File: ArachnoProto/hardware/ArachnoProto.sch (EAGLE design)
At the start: 21 parts, among them J1 PINHEAD-17-REV, J2 PINHEAD-17-REV

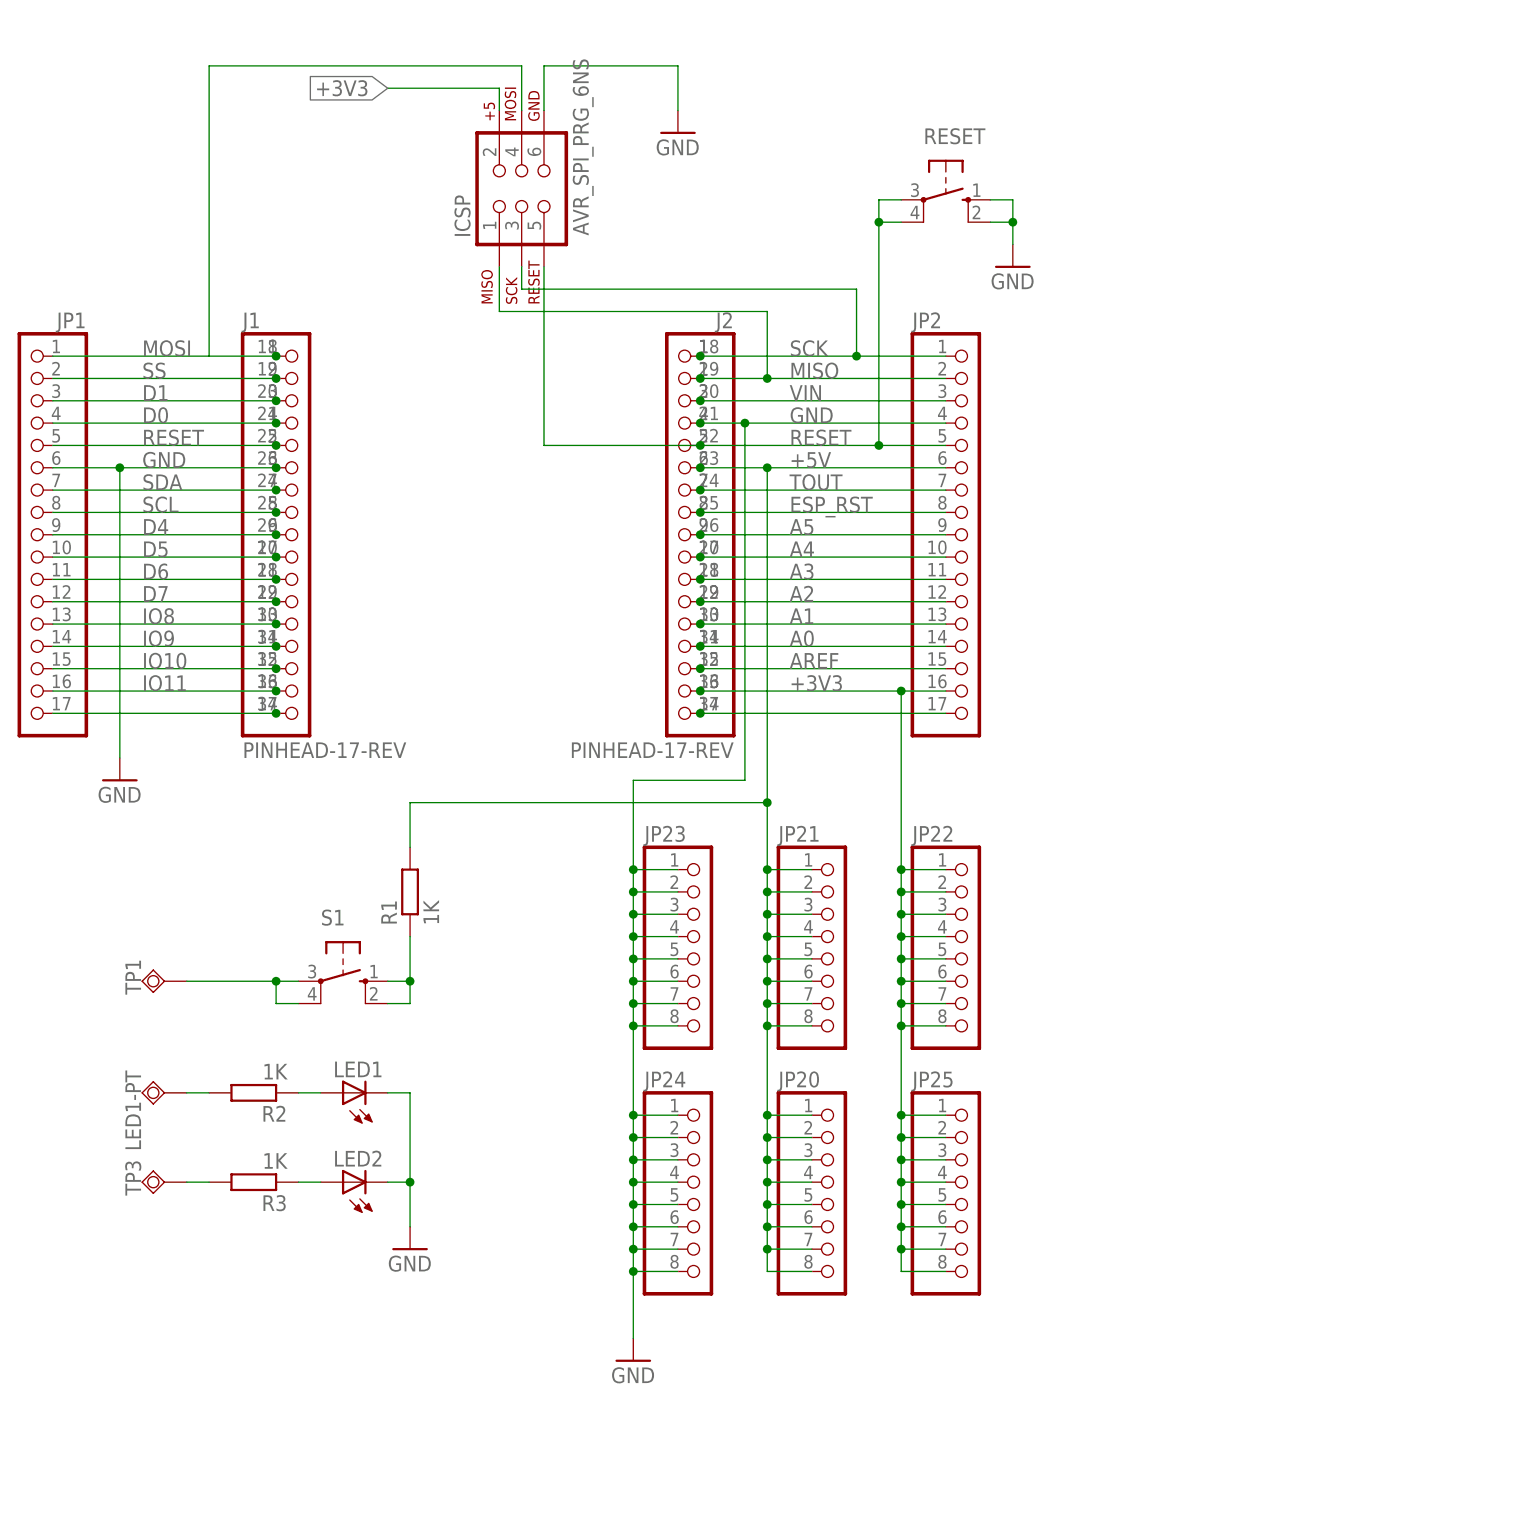
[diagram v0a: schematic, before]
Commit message: -- Added mounting pads on the board -- Made reset button an independent button -- Changed all components to SMD
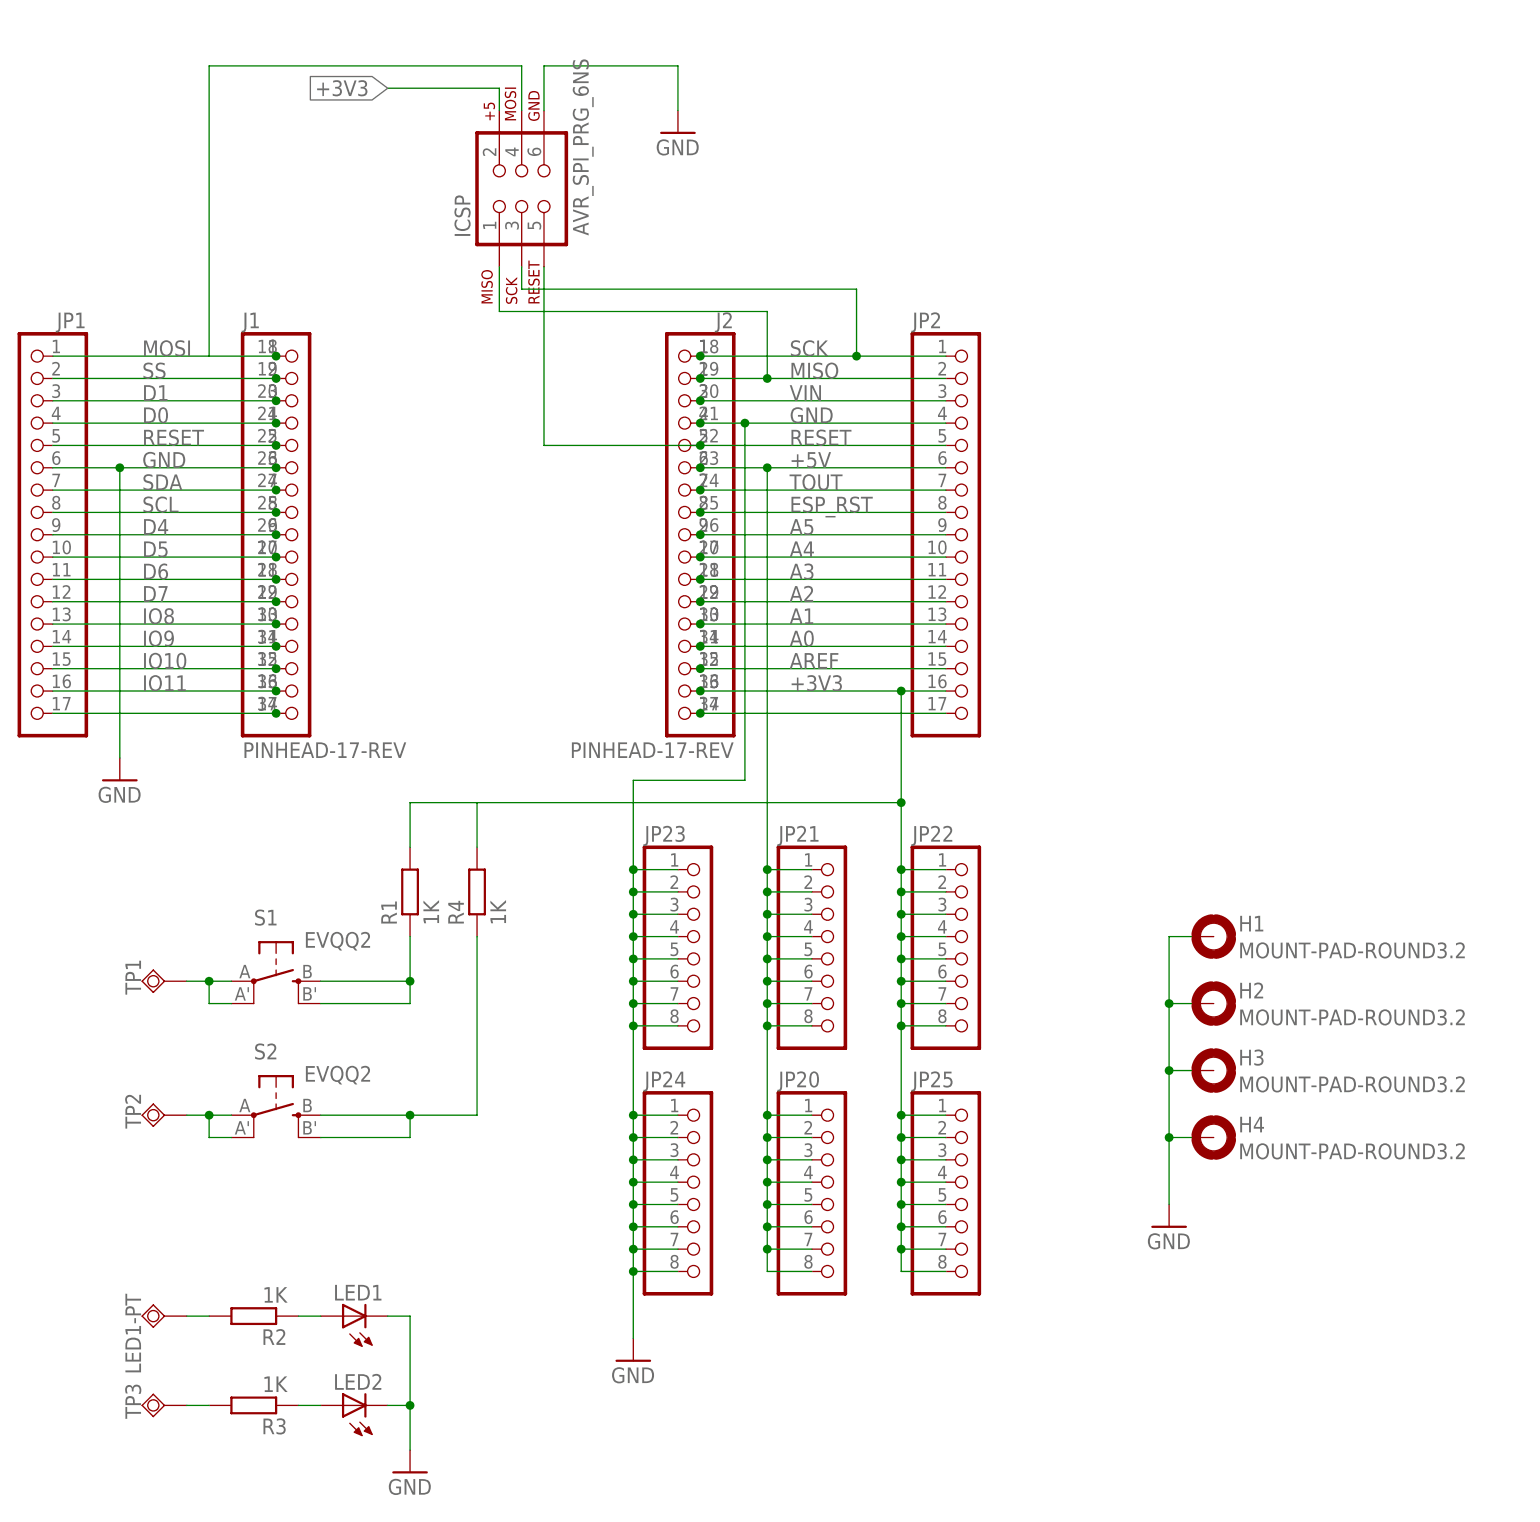
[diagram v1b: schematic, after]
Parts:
- removed RESET: (no value), switch-omron:10-XX
- added H1, H2, H3, H4: MOUNT-PAD-ROUND3.2, holes:MOUNT-PAD-ROUND3.2
- added R4: 1K, resistor:R-EU_R1206
- added S2: EVQQ2, adafruit:EVQQ2
- added TP2: TPSQPAD1-20Y, test-fixtures:TPSQPAD1-20Y
- LED1, LED2: device adafruit:LED5MM -> led:LEDCHIPLED_1206
- R1, R2, R3: device resistor:R-EU_R0603 -> resistor:R-EU_R1206
- S1: value (none) -> EVQQ2; device switch-omron:10-XX -> adafruit:EVQQ2
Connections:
- new net N$69: R4.1, S2.S, S2.S1
- new net N$70: S2.P, S2.P1, TP2.TP
- net +3V3: now also R1.2, R4.2
- net +5V: no longer R1.2
- net GND: now also H1.MOUNT, H2.MOUNT, H3.MOUNT, H4.MOUNT; no longer RESET.S, RESET.S1
- net RESET: no longer RESET.P, RESET.P1
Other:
- moved on the sheet: LED1, LED1-PT, LED2, R2, R3, TP3

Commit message: Modified ArachnoProto to work with the ArachnioDue.
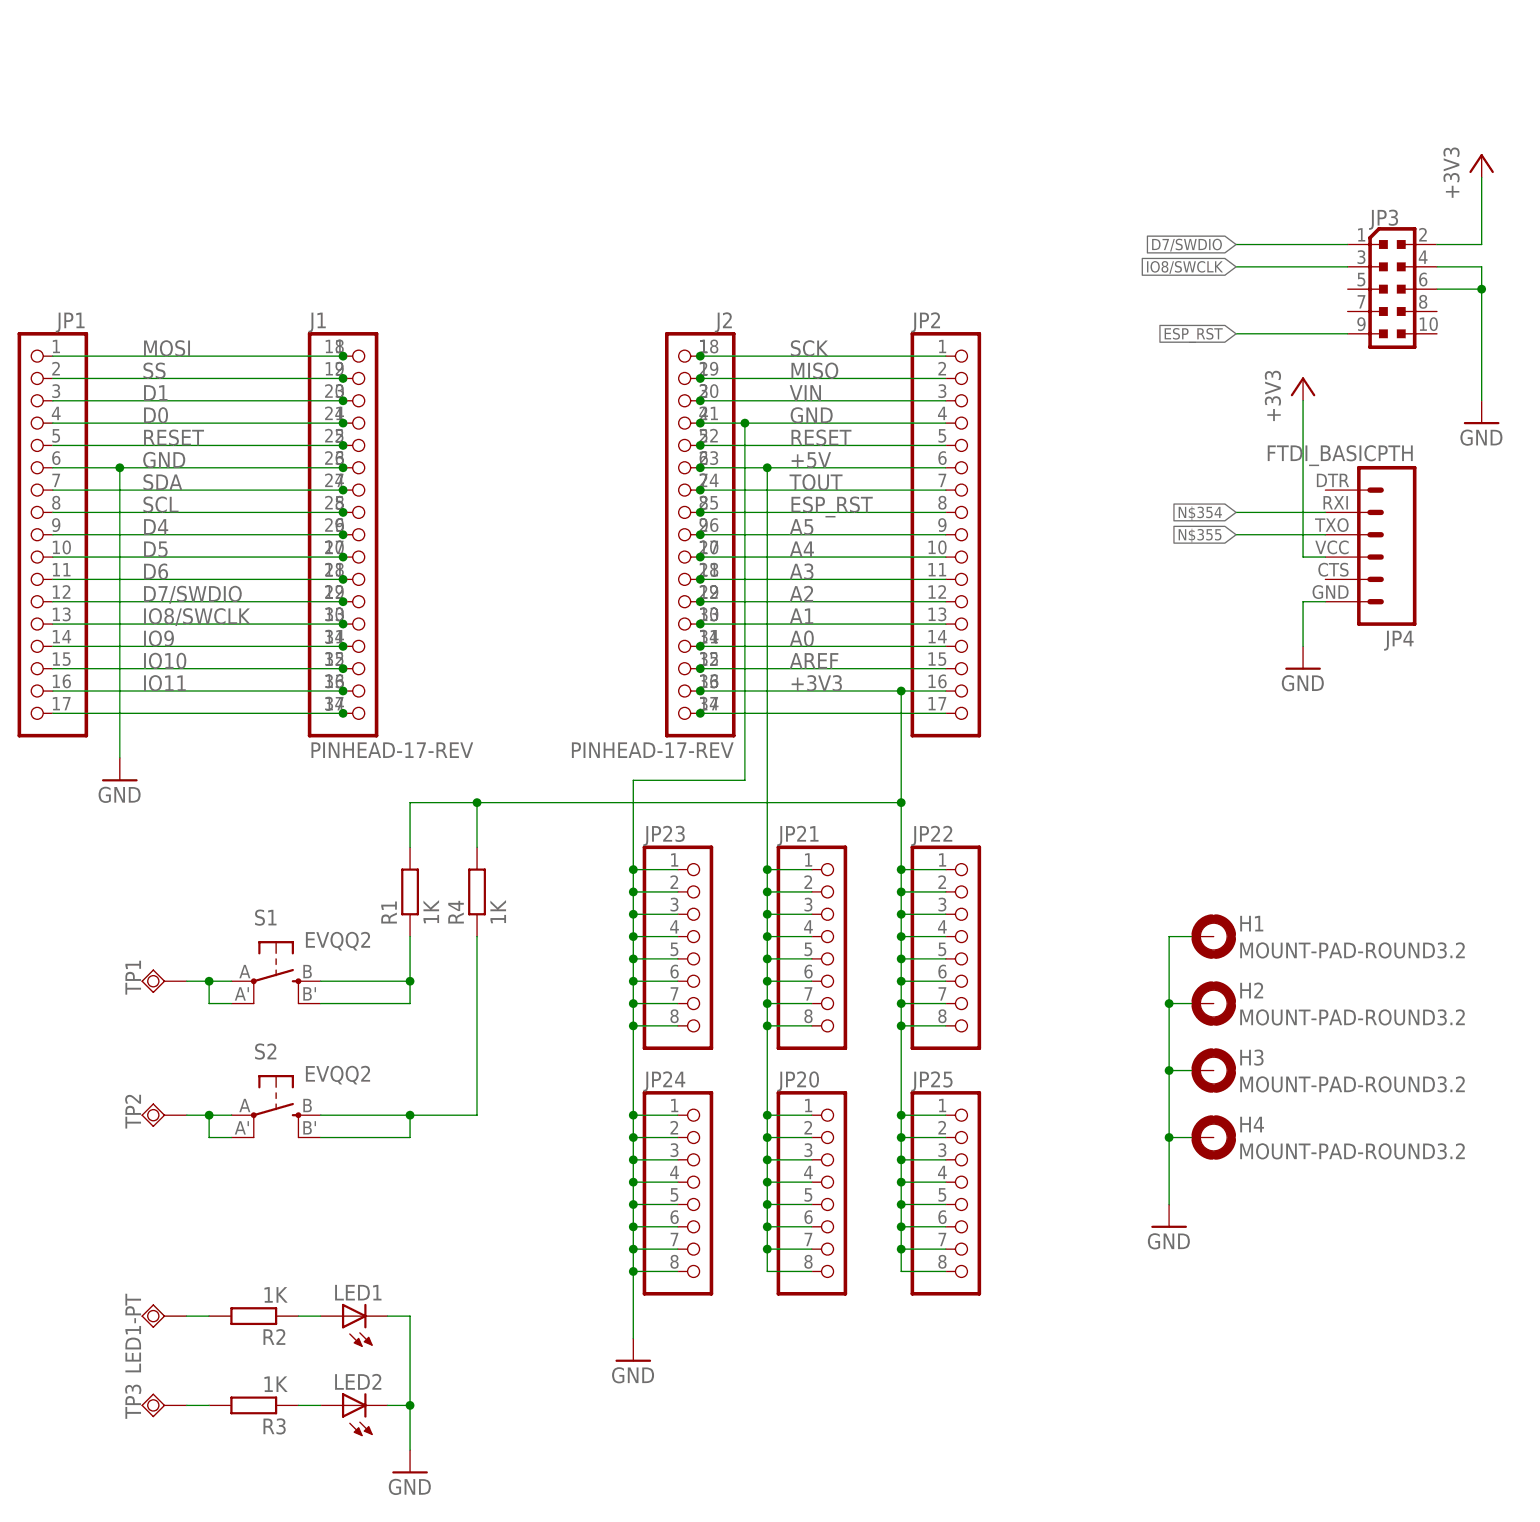
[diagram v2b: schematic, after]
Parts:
- removed ICSP: AVR_SPI_PRG_6NS, SparkFun-Connectors:AVR_SPI_PRG_6NS
- added JP3: (no value), atmel-d21:PINHEAD_PINHD-2X5PASSO127
- added JP4: FTDI_BASICPTH, SparkFun-Connectors:FTDI_BASICPTH
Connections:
- removed net D7: J1.12, J1.29, JP1.12
- removed net IO8: J1.13, J1.30, JP1.13
- new net D7/SWDIO: J1.12, J1.29, JP1.12, JP3.1
- new net IO8/SWCLK: J1.13, J1.30, JP1.13, JP3.3
- new net N$354: JP4.2
- new net N$355: JP4.3
- net +3V3: now also JP3.2, JP4.4; no longer ICSP.2
- net ESP_RST: now also JP3.9
- net GND: now also JP3.4, JP3.6, JP4.6; no longer ICSP.6
- net MISO: no longer ICSP.1
- net MOSI: no longer ICSP.4
- net RESET: no longer ICSP.5
- net SCK: no longer ICSP.3
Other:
- moved on the sheet: J1

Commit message: Modified ArachnNode to Arachnio Due standard
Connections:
- removed net N$354: JP4.2
- removed net N$355: JP4.3
- net D0: now also JP4.2
- net D1: now also JP4.3
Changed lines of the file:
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@@
 <pinref part="JP1" gate="G$1" pin="3"/>
+</segment>
+<segment>
+<pinref part="JP4" gate="G$1" pin="3"/>
+<wire x1="233.68" y1="142.24" x2="223.52" y2="142.24" width="0.1524" layer="91"/>
+<label x="223.52" y="142.24" size="1.27" layer="95" rot="R180" xref="yes"/>
 </segment>
 </net>
@@
 <junction x="121.92" y="154.94"/>
 <pinref part="JP1" gate="G$1" pin="4"/>
+</segment>
+<segment>
+<pinref part="JP4" gate="G$1" pin="2"/>
+<wire x1="233.68" y1="144.78" x2="223.52" y2="144.78" width="0.1524" layer="91"/>
+<label x="223.52" y="144.78" size="1.27" layer="95" rot="R180" xref="yes"/>
 </segment>
 </net>
@@
 </segment>
 </net>
-<net name="N$354" class="0">
-<segment>
-<pinref part="JP4" gate="G$1" pin="2"/>
-<wire x1="233.68" y1="144.78" x2="223.52" y2="144.78" width="0.1524" layer="91"/>
-<label x="223.52" y="144.78" size="1.27" layer="95" rot="R180" xref="yes"/>
-</segment>
-</net>
-<net name="N$355" class="0">
-<segment>
-<pinref part="JP4" gate="G$1" pin="3"/>
-<wire x1="233.68" y1="142.24" x2="223.52" y2="142.24" width="0.1524" layer="91"/>
-<label x="223.52" y="142.24" size="1.27" layer="95" rot="R180" xref="yes"/>
-</segment>
-</net>

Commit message: Updated Arachnoproto with fixed SWD header.
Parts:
- removed JP20, JP21: (no value), pinhead:PINHD-1X8
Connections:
- removed net +5V: J2.23, J2.6, JP2.6, JP20.1, JP20.2, JP20.3, JP20.4, JP20.5, JP20.6, JP20.7, JP20.8, JP21.1, JP21.2, JP21.3, JP21.4, JP21.5, JP21.6, JP21.7, JP21.8
- removed net N$2: J1.17, J1.34, JP1.17
- removed net N$4: J2.17, J2.34, JP2.17
- removed net TOUT: J2.24, J2.7, JP2.7
- new net ERASE: J2.24, J2.41, J2.7, JP2.7
- new net IO12: J1.17, J1.34, J1.51, JP1.17
- new net IO13: J2.17, J2.34, J2.51, JP2.17
- new net SWO/IO14: J2.25, J2.42, J2.8, JP2.8, JP3.9
- new net VCC: J2.23, J2.40, J2.6, JP2.6
- net +3V3: now also J2.50
- net A0: now also J2.48
- net A1: now also J2.47
- net A2: now also J2.46
- net A3: now also J2.45
- net A4: now also J2.44
- net A5: now also J2.43
- net AREF: now also J2.49
- net D0: now also J1.38
- net D1: now also J1.37
- net D4: now also J1.43
- net D5: now also J1.44
- net D6: now also J1.45
- net D7/SWDIO: now also J1.46
- net ESP_RST: now also J2.22, J2.39, J2.5, JP2.5; no longer J2.25, J2.8, JP2.8, JP3.9
- net GND: now also J1.40, J2.38
- net IO10: now also J1.49
- net IO11: now also J1.50
- net IO8/SWCLK: now also J1.47
- net IO9: now also J1.48
- net MISO: now also J2.36
- net MOSI: now also J1.35
- net RESET: now also J1.39; no longer J2.22, J2.5, JP2.5
- net SCK: now also J2.35
- net SCL: now also J1.42
- net SDA: now also J1.41
- net SS: now also J1.36
- net VIN: now also J2.37
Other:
- moved on the sheet: JP23, JP24
